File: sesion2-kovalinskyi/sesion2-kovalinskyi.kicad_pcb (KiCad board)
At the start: 4 copper layers, 126.1 x 73.2 mm, 29 parts, among them J1 Screw_Terminal_01x02, J2 Conn_01x06_Pin, SW1 SW_Push, U1 LD1117S33TR_SOT223, U2 ATmega328P-AU, U3 MCP9808_MSOP, U4 ADXL343

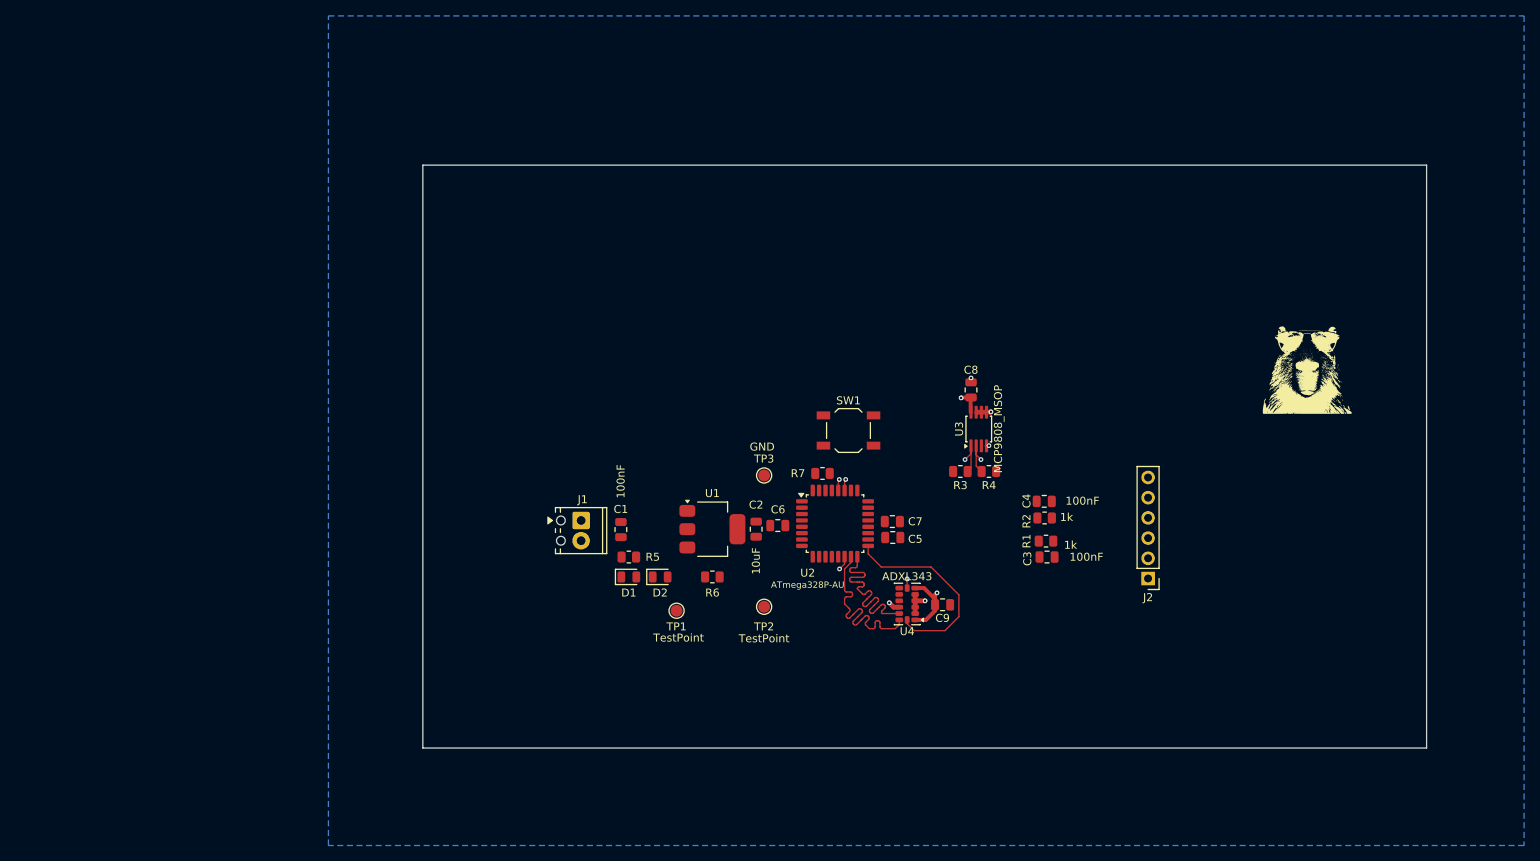
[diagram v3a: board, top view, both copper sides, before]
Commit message: Sesión 4 - Entrega Completa
- Incorporación de dos sensores en el circuito: uno bajo protocolo I2C y otro bajo protocolo SPI.
- Integración física y esquemática de conector tipo USB-C para comunicación diferencial.
- Integrado bloque USB-C con CH340C y resuelto ERC (conectado el pin V3 a +3V3 según especifica el datasheet para operación a 3,3 V, excluyendo el falso positivo de conflicto de salidas de alimentación del ERC).
- Ajuste de par diferencial (DIFF_90): el uso directo de la herramienta "Tune Skew of Differential Pair" no computa la longitud total completa de las redes al existir saltos de vía y pistas auxiliares en el conector; por ello, el ajuste de longitud se ha resuelto mediante meandros manuales y la definición de reglas personalizadas para la verificación del skew intracanal (< 0.05 mm) en el DRC.
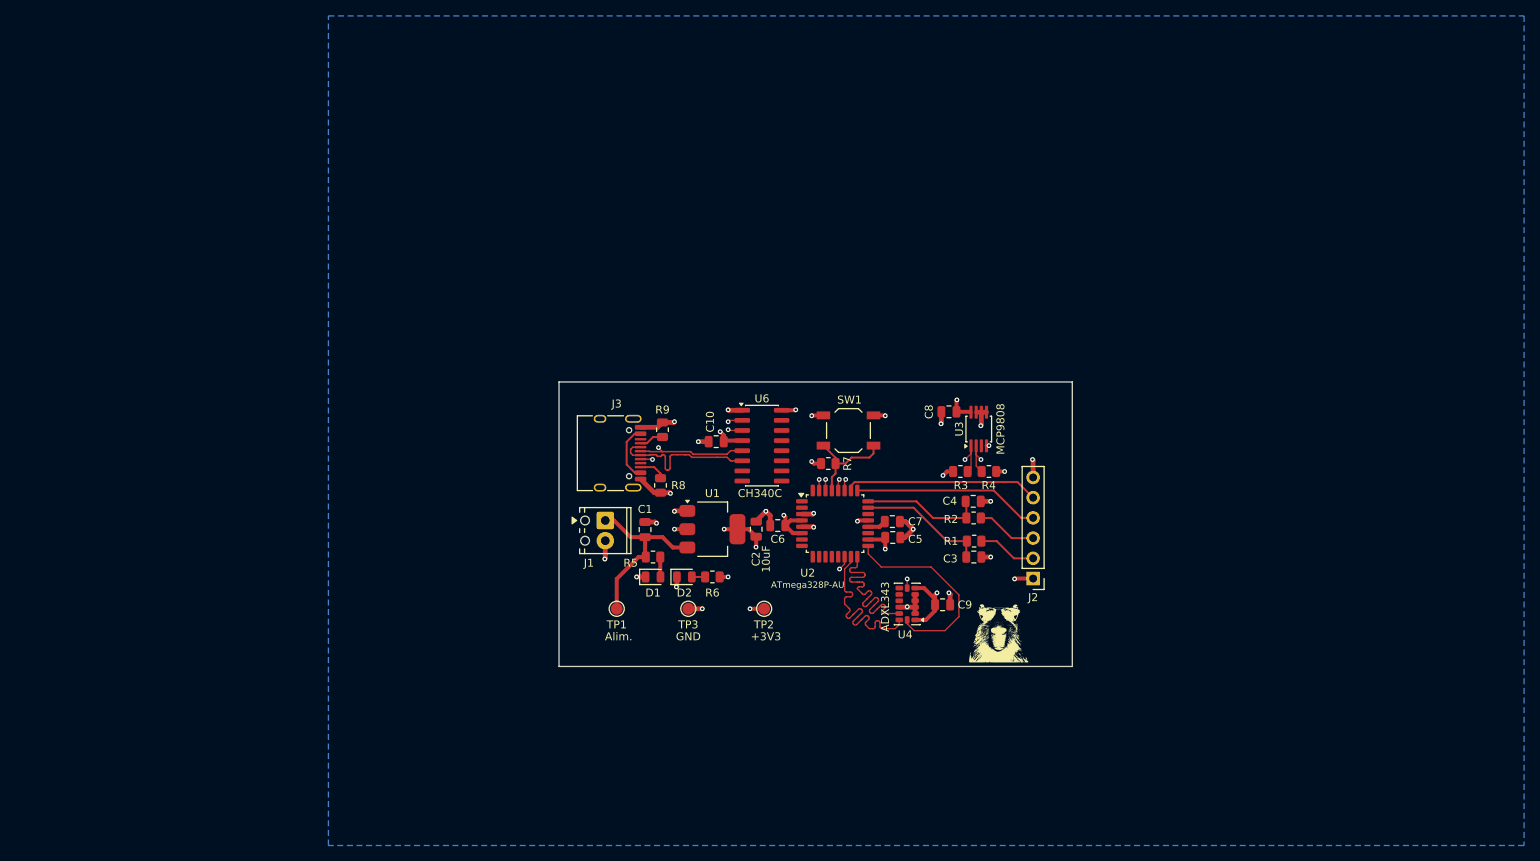
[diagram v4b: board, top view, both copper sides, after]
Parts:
- added C10: 100nF, Capacitor_SMD:C_0805_2012Metric, F.Cu at (119.0, 97.2)
- added J3: USB_C_Receptacle_USB2.0_16P, Connector_USB:USB_C_Receptacle_HRO_TYPE-C-31-M-12, F.Cu at (105.5, 98.7)
- added R8: 5.1k, Resistor_SMD:R_0805_2012Metric, F.Cu at (112.0, 102.8)
- added R9: 5.1k, Resistor_SMD:R_0805_2012Metric, F.Cu at (112.2, 95.8)
- added U6: CH340C, Package_SO:SOIC-16_3.9x9.9mm_P1.27mm, F.Cu at (124.8, 97.8)
- U3: value MCP9808_MSOP -> MCP9808
- moved G*** 51.1 mm to (154.5, 121.0)
- moved TP3 19.3 mm to (115.5, 118.2)
- moved J2 14.4 mm to (158.8, 114.5)
- moved C3 9.20 mm to (151.4, 111.8)
- moved R1 9.03 mm to (151.4, 109.8)
- moved C4 8.92 mm to (151.3, 104.8)
- moved R2 8.92 mm to (151.3, 106.8)
- moved TP1 7.53 mm to (106.5, 118.2)
- moved C8 3.91 mm to (148.2, 93.5), turned to 0 degrees
- moved C1 3.04 mm to (110.1, 108.3)
- moved D1 3.04 mm to (111.1, 114.2)
- moved D2 3.04 mm to (115.0, 114.2)
- moved J1 3.04 mm to (105.1, 107.2)
- moved R5 3.04 mm to (111.1, 111.8)
- moved R7 1.45 mm to (133.1, 100.0)
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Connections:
- net /alimentacion/+3V3 renamed /UART-USB/+3V3
- net /alimentacion/GND renamed /UART-USB/GND
- U2 pad 30: unconnected-(U2-PD0-Pad30) -> /UART-USB/MCU_RX
- U2 pad 31: unconnected-(U2-PD1-Pad31) -> /UART-USB/MCU_TX
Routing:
- net /UART-USB/GND: track 7.26 -> 52.6 mm, vias 5 -> 25
- net /UART-USB/+3V3: track 12.3 -> 44.3 mm, vias 2 -> 15
- net Net-(J2-Pin_5): track 0.00 -> 24.5 mm
- net Net-(J2-Pin_4): track 0.00 -> 23.5 mm
- net Net-(J1-Pin_1): track 0.00 -> 22.8 mm
- net /UART-USB/USB-: track 0.00 -> 19.9 mm
- net /UART-USB/MCU_RX: track 0.00 -> 18.5 mm, vias 0 -> 2
- net /UART-USB/MCU_TX: track 0.00 -> 17.2 mm, vias 0 -> 2
- net /UART-USB/USB+: track 0.00 -> 17.1 mm, vias 0 -> 2
- net Net-(U2-PC0): track 0.00 -> 16.2 mm
- net Net-(U2-PC1): track 0.00 -> 15.3 mm
- net Net-(U2-~{RESET}/PC6): track 0.00 -> 12.7 mm
- net Net-(J2-Pin_3): track 0.00 -> 7.61 mm
- net Net-(J2-Pin_2): track 0.00 -> 7.39 mm
- net /UART-USB/No Conectado: track 0.00 -> 7.20 mm
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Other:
- board size 126.1 x 73.2 mm -> 64.5 x 35.7 mm
- board text added: "+3V3"
- board text added: "Alim."

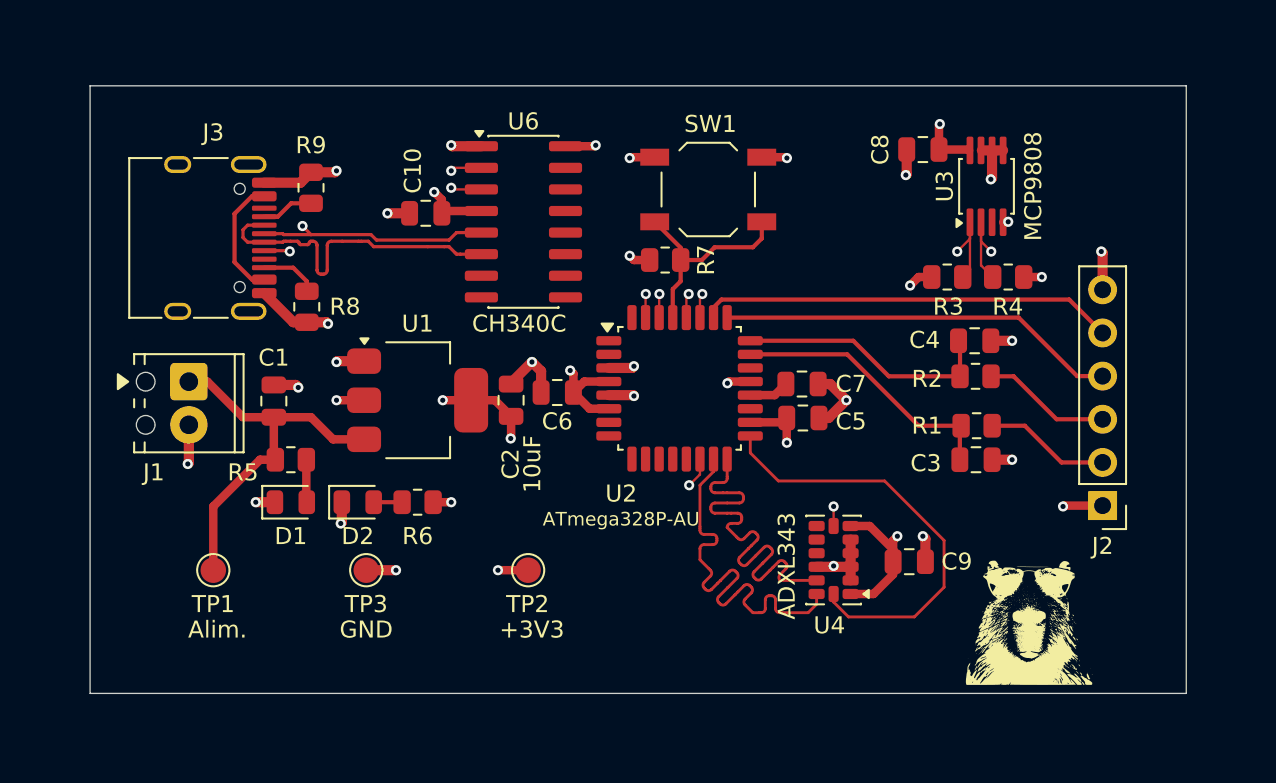
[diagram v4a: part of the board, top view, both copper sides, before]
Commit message: Apartados 1 - 3 completados; integrando protecciones (apartado 4) en el esquemático
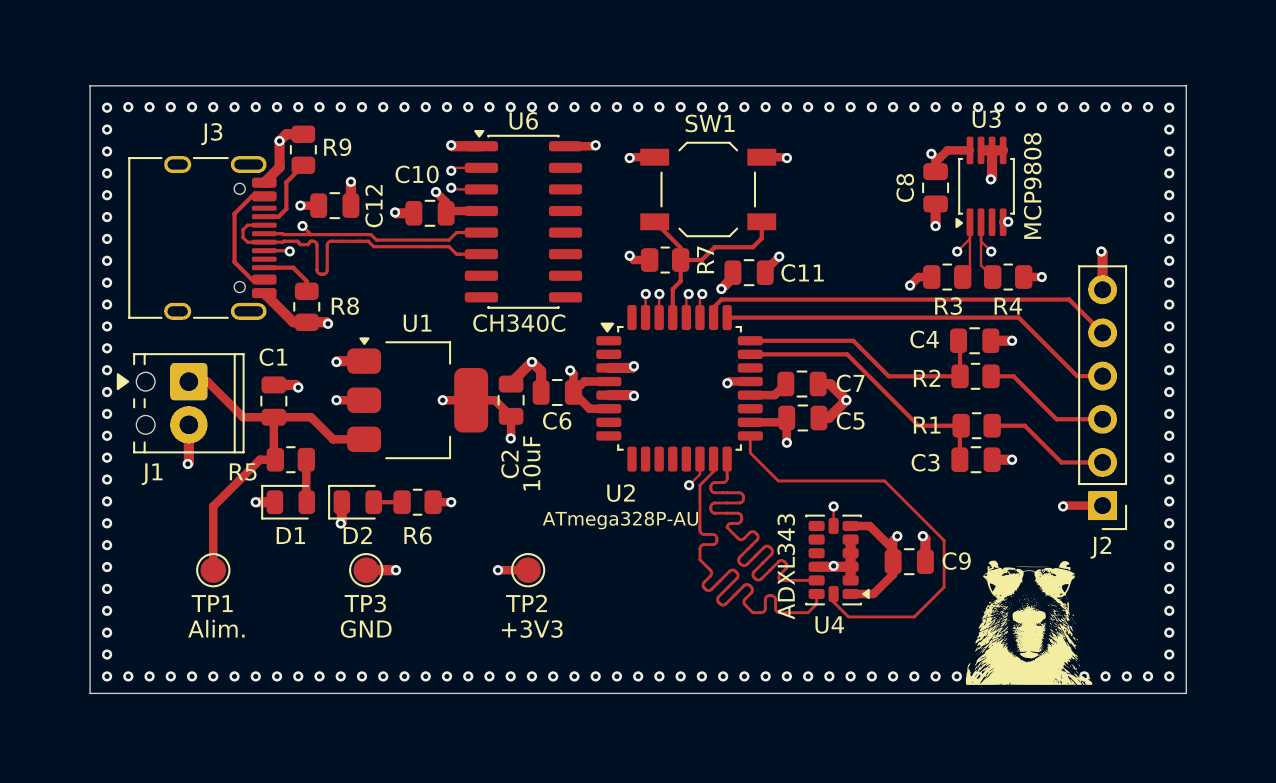
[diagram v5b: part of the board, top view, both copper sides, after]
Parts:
- added C11: 100nF, Capacitor_SMD:C_0805_2012Metric, F.Cu at (138.0, 100.7)
- added C12: 100nF, Capacitor_SMD:C_0805_2012Metric, F.Cu at (113.7, 96.8)
- moved C8 2.37 mm to (149.0, 95.8), turned to 90 degrees
- moved R9 2.28 mm to (111.8, 93.5)
- moved C10 0.25 mm to (119.2, 97.2)
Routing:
- net /UART-USB/+3V3: track 44.3 -> 47.2 mm, vias 15 -> 17
- net /UART-USB/GND: track 52.6 -> 54.9 mm, vias 25 -> 179
- net Net-(J3-CC1): track 3.08 -> 4.48 mm

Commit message: Copia de seguridad Sesión 5
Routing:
- net /microcontrolador/SCL: track 26.2 -> 25.1 mm
- net /UART-USB/GND: track 54.9 -> 55.6 mm, vias 179 -> 27

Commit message: Sesión 5 - LAYOUT FINAL (verificar Vías de Cosido)
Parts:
- added C13: 100nF, Capacitor_SMD:C_0805_2012Metric, F.Cu at (164.0, 103.5)
- added C14: 100nF, Capacitor_SMD:C_0805_2012Metric, F.Cu at (164.0, 96.4)
- added D3: D_TVS, Diode_SMD:D_SOD-123, F.Cu at (111.2, 108.7)
- added D4: D_TVS, Diode_SMD:D_SOD-123, F.Cu at (171.0, 120.2)
- added D5: D_TVS, Diode_SMD:D_SOD-123, F.Cu at (162.6, 115.8)
- added D6: D_TVS, Diode_SMD:D_SOD-123, F.Cu at (162.6, 110.1)
- added D7: D_TVS, Diode_SMD:D_SOD-123, F.Cu at (167.1, 102.9)
- added D8: D_TVS, Diode_SMD:D_SOD-123, F.Cu at (167.1, 97.0)
- added FB1: 100 Ohm @ 100MHz, Resistor_SMD:R_0805_2012Metric, F.Cu at (112.1, 114.1)
- added R10: 1k, Resistor_SMD:R_0805_2012Metric, F.Cu at (164.0, 101.5)
- added R11: 1k, Resistor_SMD:R_0805_2012Metric, F.Cu at (163.9, 98.4)
- added U5: USBLC6-2SC6, Package_TO_SOT_SMD:SOT-23-6, F.Cu at (119.5, 100.4)
- moved J2 12.3 mm to (171.1, 114.7)
- moved C3 9.23 mm to (159.3, 116.4)
- moved C4 9.23 mm to (159.3, 109.4)
- moved R1 9.23 mm to (159.4, 114.4)
- moved R2 9.23 mm to (159.3, 111.5)
- moved R5 5.48 mm to (116.0, 114.1)
- moved D1 5.38 mm to (116.0, 116.3)
- moved D2 5.38 mm to (120.0, 116.3)
- moved R6 5.38 mm to (123.5, 116.3)
- moved C1 3.80 mm to (113.7, 109.4)
- moved U6 3.65 mm to (128.4, 98.0)
- moved C10 3.65 mm to (122.9, 97.5)
- moved TP1 2.92 mm to (108.4, 120.5)
- moved TP2 2.92 mm to (126.9, 120.5)
- moved TP3 2.92 mm to (117.4, 120.5)
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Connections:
- C1 pad 2: Net-(J1-Pin_1) -> Net-(U1-VI)
- J1 pad 1: Net-(J1-Pin_1) -> Net-(D3-A1)
- J2 pad 4: Net-(J2-Pin_4) -> Net-(D7-A2)
- J2 pad 5: Net-(J2-Pin_5) -> Net-(D8-A2)
- J3 pad A6: /UART-USB/USB+ -> /UART-USB/C_USB+
- J3 pad A7: /UART-USB/USB- -> /UART-USB/C_USB-
- J3 pad B6: /UART-USB/USB+ -> /UART-USB/C_USB+
- J3 pad B7: /UART-USB/USB- -> /UART-USB/C_USB-
- R5 pad 2: Net-(J1-Pin_1) -> Net-(U1-VI)
- TP1 pad 1: Net-(J1-Pin_1) -> Net-(U1-VI)
- U1 pad 3: Net-(J1-Pin_1) -> Net-(U1-VI)
- U2 pad 25: Net-(J2-Pin_4) -> /microcontrolador/PIN_25
- U2 pad 26: Net-(J2-Pin_5) -> /microcontrolador/PIN_26
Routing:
- net /microcontrolador/PIN_26: track 0.00 -> 31.6 mm
- net /microcontrolador/PIN_25: track 0.00 -> 28.1 mm
- net Net-(J2-Pin_5): track 24.5 -> 0.00 mm
- net Net-(J2-Pin_4): track 23.5 -> 0.00 mm
- net Net-(J1-Pin_1): track 22.8 -> 0.00 mm
- net Net-(U1-VI): track 0.00 -> 16.7 mm
- net /UART-USB/GND: track 55.6 -> 70.3 mm, vias 27 -> 208
- net /UART-USB/C_USB-: track 0.00 -> 14.1 mm
- net /UART-USB/USB-: track 19.6 -> 5.87 mm
- net /UART-USB/C_USB+: track 0.00 -> 11.4 mm, vias 0 -> 2
- net /UART-USB/USB+: track 16.9 -> 5.86 mm, vias 2 -> 0
- net Net-(D7-A2): track 0.00 -> 10.4 mm
- net Net-(D8-A2): track 0.00 -> 9.91 mm
- net Net-(D3-A1): track 0.00 -> 9.75 mm
- net /UART-USB/+3V3: track 47.2 -> 56.0 mm
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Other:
- board size 64.5 x 35.7 mm -> 75 x 38 mm

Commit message: Sesión 5 - ENTREGA FINAL
Se han cumplido todos los apartados
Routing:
- added copper zone on F.Cu, net /UART-USB/GND
